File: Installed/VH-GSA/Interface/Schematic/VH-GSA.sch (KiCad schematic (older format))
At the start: 0 parts

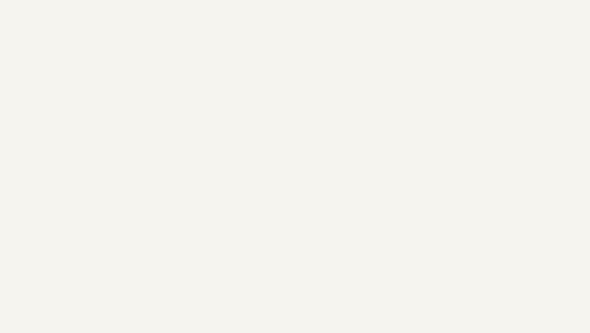
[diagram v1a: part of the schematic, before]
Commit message: VH-GSA: Removed Flarm loop through
This version assumes that the Flatm Redbox is connected to the S8
Vario.
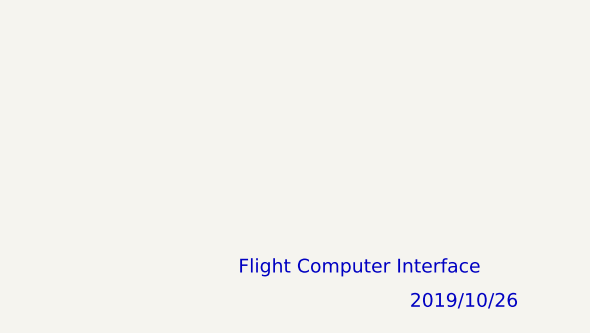
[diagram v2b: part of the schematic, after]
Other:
- note added: "2019/10/26"
- note added: "Flight Computer Interface"
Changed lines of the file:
@@
 F1 "Power.sch" 60
 $EndSheet
+Text Notes 7400 7500 0    60   ~ 0
+Flight Computer Interface
+Text Notes 8150 7650 0    60   ~ 0
+2019/10/26
 $EndSCHEMATC
